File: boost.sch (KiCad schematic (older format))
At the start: 11 parts, among them SW201 SW_SPST, U201 TPS61022

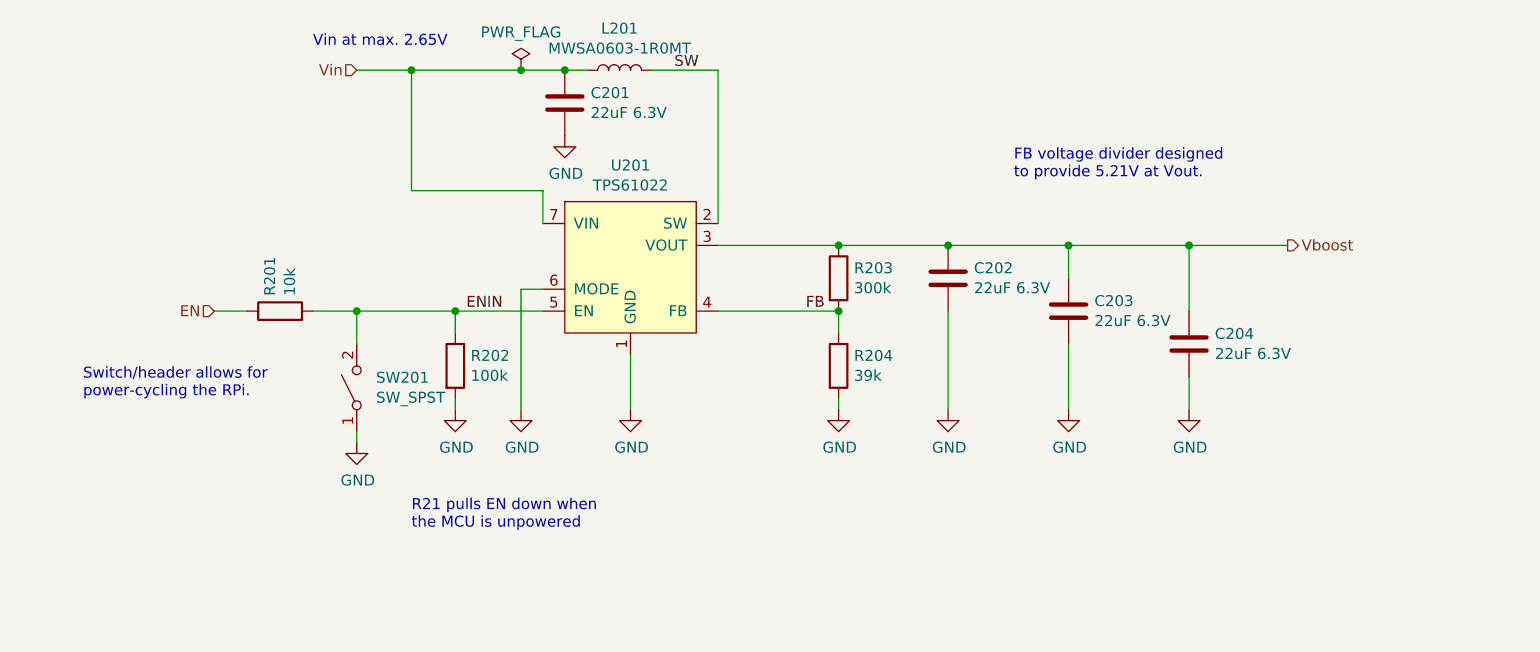
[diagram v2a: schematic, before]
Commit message: Redesigned layout to take EMC issues better into account
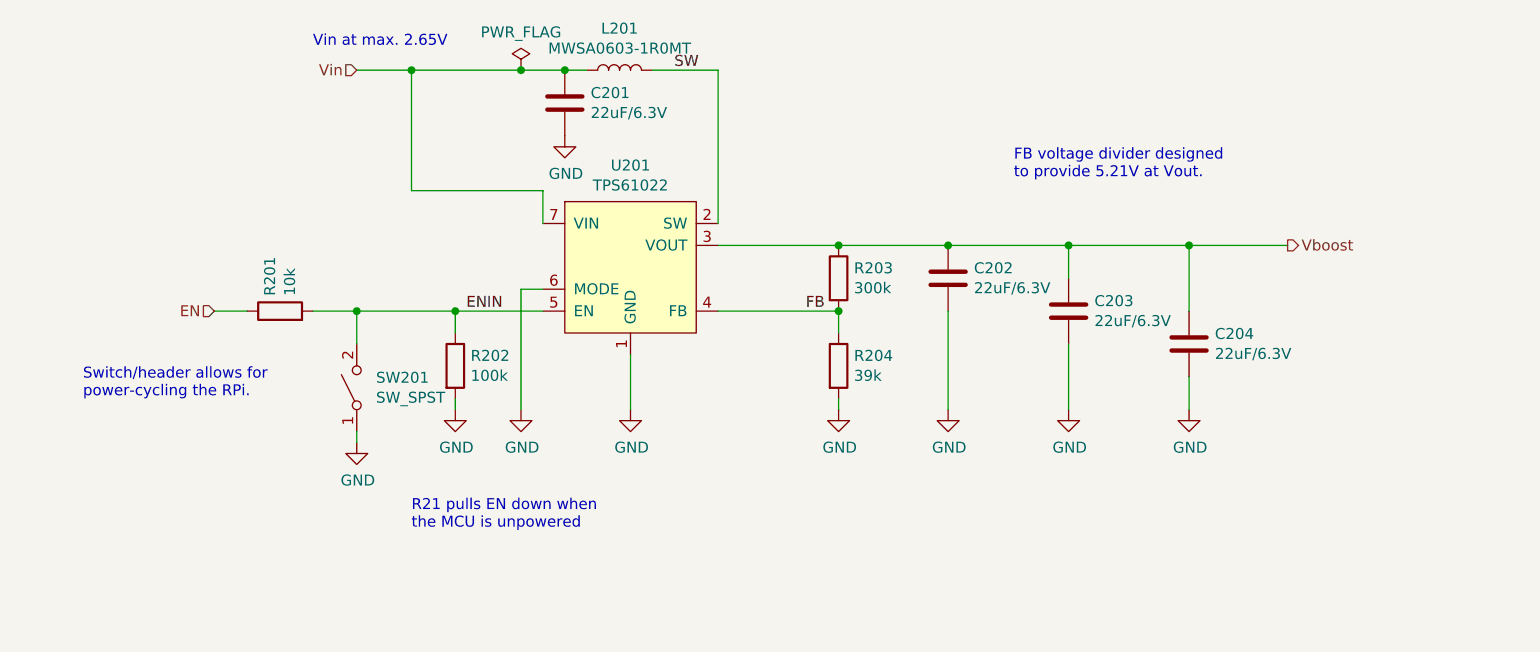
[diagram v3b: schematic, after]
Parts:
- C201, C202, C203, C204: value 22uF 6.3V -> 22uF/6.3V
- R201: footprint Resistor_SMD:R_0603_1608Metric -> Resistor_SMD:R_0402_1005Metric; LCSC C25804 -> C25744
- R202: footprint Resistor_SMD:R_0603_1608Metric -> Resistor_SMD:R_0402_1005Metric; LCSC C25803 -> C25741
- R203: footprint Resistor_SMD:R_0603_1608Metric -> Resistor_SMD:R_0402_1005Metric; LCSC C23024 -> C25774
- R204: footprint Resistor_SMD:R_0603_1608Metric -> Resistor_SMD:R_0402_1005Metric; LCSC C23153 -> C25783
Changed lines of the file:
@@
 $Descr A4 11693 8268
 encoding utf-8
-Sheet 2 8
+Sheet 2 9
 Title "Sailor Hat for Raspberry Pi"
 Date ""
@@
 AR Path="/5CA73F16/5CA6B4E8" Ref="C202"  Part="1"
 F 0 "C202" H 4968 2496 50  0000 L CNN
-F 1 "22uF 6.3V" H 4968 2405 50  0000 L CNN
+F 1 "22uF/6.3V" H 4968 2405 50  0000 L CNN
 F 2 "Capacitor_SMD:C_0805_2012Metric" H 4888 2300 50  0001 C CNN
 F 3 "~" H 4850 2450 50  0001 C CNN
@@
 F 0 "R203" H 4420 2496 50  0000 L CNN
 F 1 "300k" H 4420 2405 50  0000 L CNN
-F 2 "Resistor_SMD:R_0603_1608Metric" V 4280 2450 50  0001 C CNN
+F 2 "Resistor_SMD:R_0402_1005Metric" V 4280 2450 50  0001 C CNN
 F 3 "~" H 4350 2450 50  0001 C CNN
-F 4 "C23024" H 4350 2450 50  0001 C CNN "LCSC"
+F 4 "C25774" H 4350 2450 50  0001 C CNN "LCSC"
 	1    4350 2450
 	1    0    0    -1
@@
 F 0 "R204" H 4420 2896 50  0000 L CNN
 F 1 "39k" H 4420 2805 50  0000 L CNN
-F 2 "Resistor_SMD:R_0603_1608Metric" V 4280 2850 50  0001 C CNN
+F 2 "Resistor_SMD:R_0402_1005Metric" V 4280 2850 50  0001 C CNN
 F 3 "~" H 4350 2850 50  0001 C CNN
-F 4 "C23153" H 4350 2850 50  0001 C CNN "LCSC"
+F 4 "C25783" H 4350 2850 50  0001 C CNN "LCSC"
 	1    4350 2850
 	1    0    0    -1
@@
 AR Path="/5CA73F16/5CF608F8" Ref="C201"  Part="1"
 F 0 "C201" H 3218 1696 50  0000 L CNN
-F 1 "22uF 6.3V" H 3218 1605 50  0000 L CNN
+F 1 "22uF/6.3V" H 3218 1605 50  0000 L CNN
 F 2 "Capacitor_SMD:C_0805_2012Metric" H 3138 1500 50  0001 C CNN
 F 3 "~" H 3100 1650 50  0001 C CNN
@@
 F 0 "R201" H 1870 2646 50  0000 L CNN
 F 1 "10k" H 1870 2555 50  0000 L CNN
-F 2 "Resistor_SMD:R_0603_1608Metric" V 1730 2600 50  0001 C CNN
+F 2 "Resistor_SMD:R_0402_1005Metric" V 1730 2600 50  0001 C CNN
 F 3 "~" H 1800 2600 50  0001 C CNN
-F 4 "C25804" H 1800 2600 50  0001 C CNN "LCSC"
+F 4 "C25744" H 1800 2600 50  0001 C CNN "LCSC"
 	1    1800 2600
 	0    -1   -1   0
@@
 AR Path="/5CA73F16/5D8155D9" Ref="C203"  Part="1"
 F 0 "C203" H 5518 2646 50  0000 L CNN
-F 1 "22uF 6.3V" H 5518 2555 50  0000 L CNN
+F 1 "22uF/6.3V" H 5518 2555 50  0000 L CNN
 F 2 "Capacitor_SMD:C_0805_2012Metric" H 5438 2450 50  0001 C CNN
 F 3 "~" H 5400 2600 50  0001 C CNN
@@
 AR Path="/5CA73F16/5E6767E0" Ref="C204"  Part="1"
 F 0 "C204" H 6068 2796 50  0000 L CNN
-F 1 "22uF 6.3V" H 6068 2705 50  0000 L CNN
+F 1 "22uF/6.3V" H 6068 2705 50  0000 L CNN
 F 2 "Capacitor_SMD:C_0805_2012Metric" H 5988 2600 50  0001 C CNN
 F 3 "~" H 5950 2750 50  0001 C CNN
@@
 F 0 "R202" H 2670 2896 50  0000 L CNN
 F 1 "100k" H 2670 2805 50  0000 L CNN
-F 2 "Resistor_SMD:R_0603_1608Metric" V 2530 2850 50  0001 C CNN
+F 2 "Resistor_SMD:R_0402_1005Metric" V 2530 2850 50  0001 C CNN
 F 3 "~" H 2600 2850 50  0001 C CNN
-F 4 "C25803" H 2600 2850 50  0001 C CNN "LCSC"
+F 4 "C25741" H 2600 2850 50  0001 C CNN "LCSC"
 	1    2600 2850
 	1    0    0    -1

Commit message: Rename project files to follow the conventions in SH-ESP32
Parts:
- U201: footprint custom:TPS61022RWUR -> SH-RPi:TPS61022RWUR; symbol sailor-hat-rescue:TPS61022-sailor-hat -> SH-RPi:TPS61022
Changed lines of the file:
@@
 $EndComp
 $Comp
-L sailor-hat-rescue:TPS61022-sailor-hat U201
+L SH-RPi:TPS61022 U201
 U 1 1 5D5AC086
 P 3400 2400
 F 0 "U201" H 3400 2865 50  0000 C CNN
 F 1 "TPS61022" H 3400 2774 50  0000 C CNN
-F 2 "custom:TPS61022RWUR" H 3450 2600 50  0001 C CNN
+F 2 "SH-RPi:TPS61022RWUR" H 3450 2600 50  0001 C CNN
 F 3 "" H 3450 2600 50  0001 C CNN
 F 4 "595-TPS61022RWUR" H 3400 2400 50  0001 C CNN "Mouser"

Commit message: Extend the PCB size to provide space for an onboard supercapacitor
The PCB was extended to the left by 21mm to provide room for a
18x40mm (max 18x42mm) 50/60F supercapacitor. The supercapacitor
is lodged in a slot on the PCB to provide mechanical stability and limit
the maximum height of the assembly. It now requires 14mm of headroom.

Additionally, the following changes were made:

- the external supercap connector was removed
- the power and CAN connectors were swapped to JST XH
- there is space for a wire link between CAN and power conx
- power protection circuitry was moved to the edge of the board
- 3.3V regulator was moved to improve the layout
- a 100pF cap was added to the boost feedback to improve loop stability
- rectangles were drawn around ground pins on the GPIO connector
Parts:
- added C205: 100pF, Capacitor_SMD:C_0402_1005Metric, symbol Device:C
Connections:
- wire segments 33 -> 35
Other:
- note added: "C205 sets an additional feedforward\nzero frequency at 5.3 kHz"
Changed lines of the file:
@@
 Title "Sailor Hat for Raspberry Pi"
 Date ""
-Rev "revL"
+Rev "revM"
 Comp "Hat Laboratories"
 Comment1 "https://creativecommons.org/licenses/by-sa/4.0"
@@
 Text HLabel 2150 1500 0    50   Input ~ 0
 Vin
-Text Notes 5150 2000 0    50   ~ 0
+Text Notes 4250 1800 0    50   ~ 0
 FB voltage divider designed\nto provide 5.21V at Vout.
 Text HLabel 6400 2300 2    50   Output ~ 0
@@
 R21 pulls EN down when\nthe MCU is unpowered
 Wire Wire Line
-	3800 2300 4350 2300
-Wire Wire Line
-	3800 2600 4350 2600
+	3800 2300 4100 2300
+Wire Wire Line
+	3800 2600 4100 2600
 Wire Wire Line
 	4350 3000 4350 3050
+$Comp
+L Device:C C205
+U 1 1 5FD0AA6F
+P 4100 2450
+F 0 "C205" H 3986 2404 50  0000 R CNN
+F 1 "100pF" H 3986 2495 50  0000 R CNN
+F 2 "Capacitor_SMD:C_0402_1005Metric" H 4138 2300 50  0001 C CNN
+F 3 "~" H 4100 2450 50  0001 C CNN
+F 4 "C1546" H 4100 2450 50  0001 C CNN "LCSC"
+	1    4100 2450
+	1    0    0    1
+$EndComp
+Connection ~ 4100 2600
+Wire Wire Line
+	4100 2600 4350 2600
+Connection ~ 4100 2300
+Wire Wire Line
+	4100 2300 4350 2300
+Text Notes 4000 2150 0    50   ~ 0
+C205 sets an additional feedforward\nzero frequency at 5.3 kHz
 $EndSCHEMATC

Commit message: Route I2C to unique pins
Also:
- Connect RTC interrupt to ATtiny
- Break out the interrupt pin to a connector for external signaling
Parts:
- added C206: 1uF, Resistor_SMD:R_0402_1005Metric, symbol Device:C
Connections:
- wire segments 35 -> 38
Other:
- note added: "C206 limits switch bouncing and slows\nreset on poweron"
- note added: "R202 pulls EN down when\nthe MCU is unpowered"
- note removed: "R21 pulls EN down when\nthe MCU is unpowered"
- moved on the sheet: R201, SW201
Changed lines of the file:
@@
 	1    0    0    -1
 $EndComp
-Text HLabel 1500 2600 0    50   Input ~ 0
+Text HLabel 1200 2600 0    50   Input ~ 0
 EN
 $Comp
@@
 $EndComp
 Wire Wire Line
-	1500 2600 1650 2600
+	1200 2600 1350 2600
 $Comp
 L power:GND #PWR?
@@
 L Switch:SW_SPST SW201
 U 1 1 5D5B325B
-P 2150 2950
-F 0 "SW201" V 2196 2862 50  0000 R CNN
-F 1 "SW_SPST" V 2105 2862 50  0000 R CNN
-F 2 "Connector_PinHeader_2.54mm:PinHeader_1x02_P2.54mm_Vertical" H 2150 2950 50  0001 C CNN
-F 3 "~" H 2150 2950 50  0001 C CNN
-	1    2150 2950
+P 1850 2950
+F 0 "SW201" V 1896 2862 50  0000 R CNN
+F 1 "SW_SPST" V 1805 2862 50  0000 R CNN
+F 2 "Connector_PinHeader_2.54mm:PinHeader_1x02_P2.54mm_Vertical" H 1850 2950 50  0001 C CNN
+F 3 "~" H 1850 2950 50  0001 C CNN
+	1    1850 2950
 	0    -1   -1   0
 $EndComp
@@
 L Device:R R?
 U 1 1 5D5B16A2
-P 1800 2600
+P 1500 2600
 AR Path="/5D5B16A2" Ref="R?"  Part="1"
 AR Path="/5C3480BB/5D5B16A2" Ref="R?"  Part="1"
 AR Path="/5CA73F16/5D5B16A2" Ref="R201"  Part="1"
-F 0 "R201" H 1870 2646 50  0000 L CNN
-F 1 "10k" H 1870 2555 50  0000 L CNN
-F 2 "Resistor_SMD:R_0402_1005Metric" V 1730 2600 50  0001 C CNN
-F 3 "~" H 1800 2600 50  0001 C CNN
-F 4 "C25744" H 1800 2600 50  0001 C CNN "LCSC"
-	1    1800 2600
+F 0 "R201" H 1570 2646 50  0000 L CNN
+F 1 "10k" H 1570 2555 50  0000 L CNN
+F 2 "Resistor_SMD:R_0402_1005Metric" V 1430 2600 50  0001 C CNN
+F 3 "~" H 1500 2600 50  0001 C CNN
+F 4 "C25744" H 1500 2600 50  0001 C CNN "LCSC"
+	1    1500 2600
 	0    -1   -1   0
 $EndComp
 Wire Wire Line
-	1950 2600 2150 2600
-Wire Wire Line
-	2150 2750 2150 2600
-Connection ~ 2150 2600
+	1650 2600 1850 2600
+Wire Wire Line
+	1850 2750 1850 2600
+Connection ~ 1850 2600
 $Comp
 L power:GND #PWR?
 U 1 1 5D5B5E50
-P 2150 3200
+P 1850 3200
 AR Path="/5D5B5E50" Ref="#PWR?"  Part="1"
 AR Path="/5C3480BB/5D5B5E50" Ref="#PWR?"  Part="1"
 AR Path="/5CA73F16/5D5B5E50" Ref="#PWR0201"  Part="1"
-F 0 "#PWR0201" H 2150 2950 50  0001 C CNN
-F 1 "GND" H 2155 3027 50  0000 C CNN
-F 2 "" H 2150 3200 50  0001 C CNN
-F 3 "" H 2150 3200 50  0001 C CNN
-	1    2150 3200
-	1    0    0    -1
-$EndComp
-Wire Wire Line
-	2150 3200 2150 3150
+F 0 "#PWR0201" H 1850 2950 50  0001 C CNN
+F 1 "GND" H 1855 3027 50  0000 C CNN
+F 2 "" H 1850 3200 50  0001 C CNN
+F 3 "" H 1850 3200 50  0001 C CNN
+	1    1850 3200
+	1    0    0    -1
+$EndComp
+Wire Wire Line
+	1850 3200 1850 3150
 $Comp
 L Device:C C?
@@
 Wire Wire Line
 	4850 3050 4850 2600
-Text Notes 900  3000 0    50   ~ 0
+Text Notes 600  3000 0    50   ~ 0
 Switch/header allows for\npower-cycling the RPi.
-Wire Wire Line
-	2150 2600 2600 2600
 Wire Wire Line
 	2400 2050 3000 2050
@@
 	2600 3000 2600 3050
 Text Notes 2400 3600 0    50   ~ 0
-R21 pulls EN down when\nthe MCU is unpowered
+R202 pulls EN down when\nthe MCU is unpowered
 Wire Wire Line
 	3800 2300 4100 2300
@@
 Text Notes 4000 2150 0    50   ~ 0
 C205 sets an additional feedforward\nzero frequency at 5.3 kHz
+$Comp
+L Device:C C206
+U 1 1 5FDD2F9B
+P 2300 2850
+F 0 "C206" H 2415 2896 50  0000 L CNN
+F 1 "1uF" H 2415 2805 50  0000 L CNN
+F 2 "Resistor_SMD:R_0402_1005Metric" H 2338 2700 50  0001 C CNN
+F 3 "~" H 2300 2850 50  0001 C CNN
+F 4 "C52923" H 2300 2850 50  0001 C CNN "LCSC"
+	1    2300 2850
+	1    0    0    -1
+$EndComp
+Wire Wire Line
+	2300 2700 2300 2600
+Connection ~ 2300 2600
+Wire Wire Line
+	2300 2600 2600 2600
+$Comp
+L power:GND #PWR?
+U 1 1 5FDD7BA3
+P 2300 3050
+AR Path="/5FDD7BA3" Ref="#PWR?"  Part="1"
+AR Path="/5C3480BB/5FDD7BA3" Ref="#PWR?"  Part="1"
+AR Path="/5CA73F16/5FDD7BA3" Ref="#PWR0210"  Part="1"
+F 0 "#PWR0210" H 2300 2800 50  0001 C CNN
+F 1 "GND" H 2305 2877 50  0000 C CNN
+F 2 "" H 2300 3050 50  0001 C CNN
+F 3 "" H 2300 3050 50  0001 C CNN
+	1    2300 3050
+	1    0    0    -1
+$EndComp
+Wire Wire Line
+	2300 3050 2300 3000
+Wire Wire Line
+	1850 2600 2300 2600
+Text Notes 2400 3850 0    50   ~ 0
+C206 limits switch bouncing and slows\nreset on poweron
 $EndSCHEMATC
